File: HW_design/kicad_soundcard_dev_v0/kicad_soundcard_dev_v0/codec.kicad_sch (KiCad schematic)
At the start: 54 parts, among them J8 PJ31060-I, J9 PJ31060-I, Q3 BSS138LT3G, Q4 BSS138LT3G, U6 ES8388

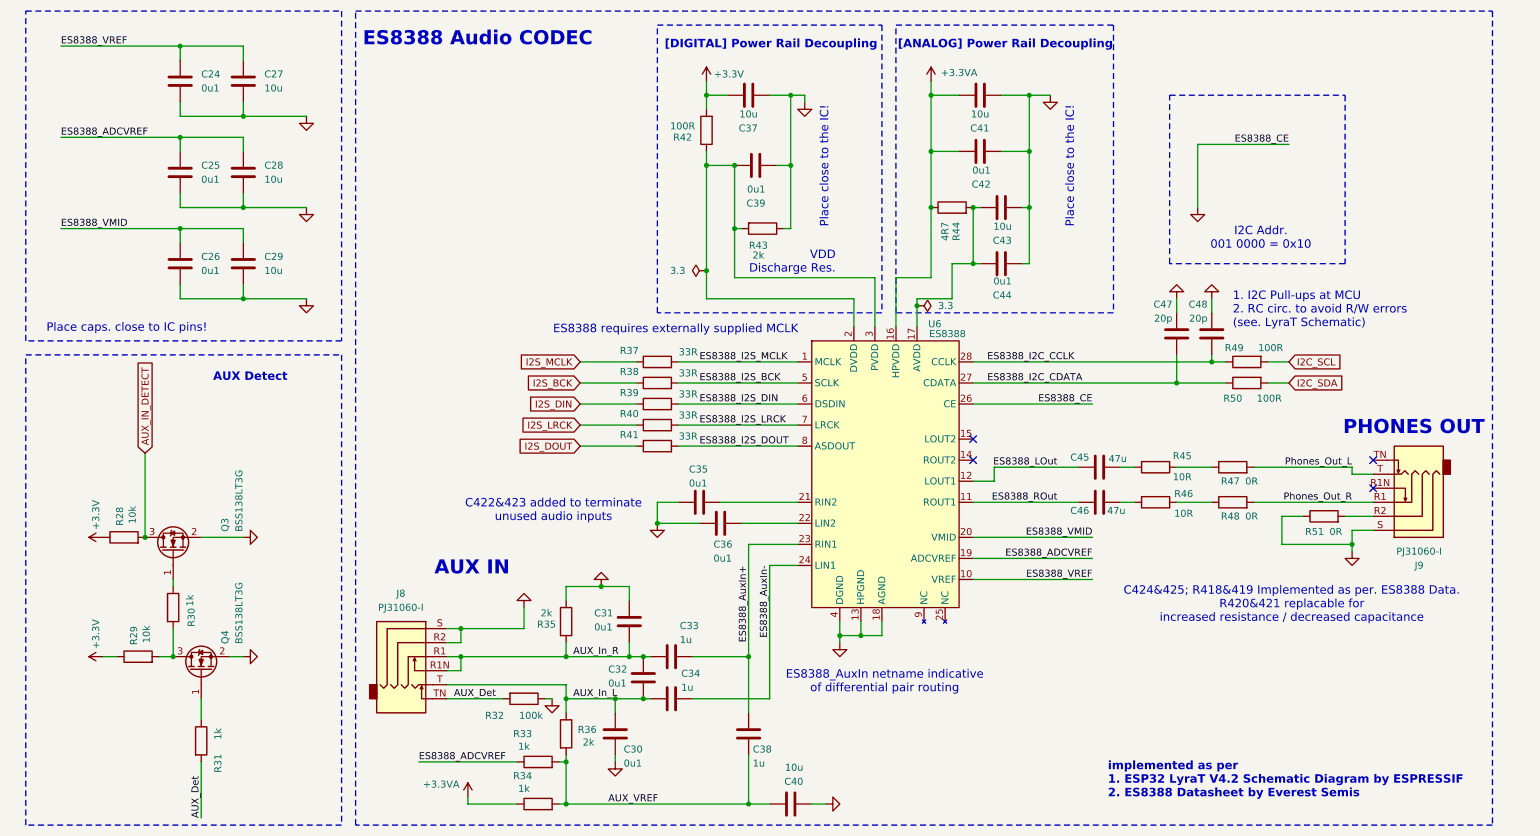
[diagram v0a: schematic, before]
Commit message: Schematic Rev2 + PCB Initial Release
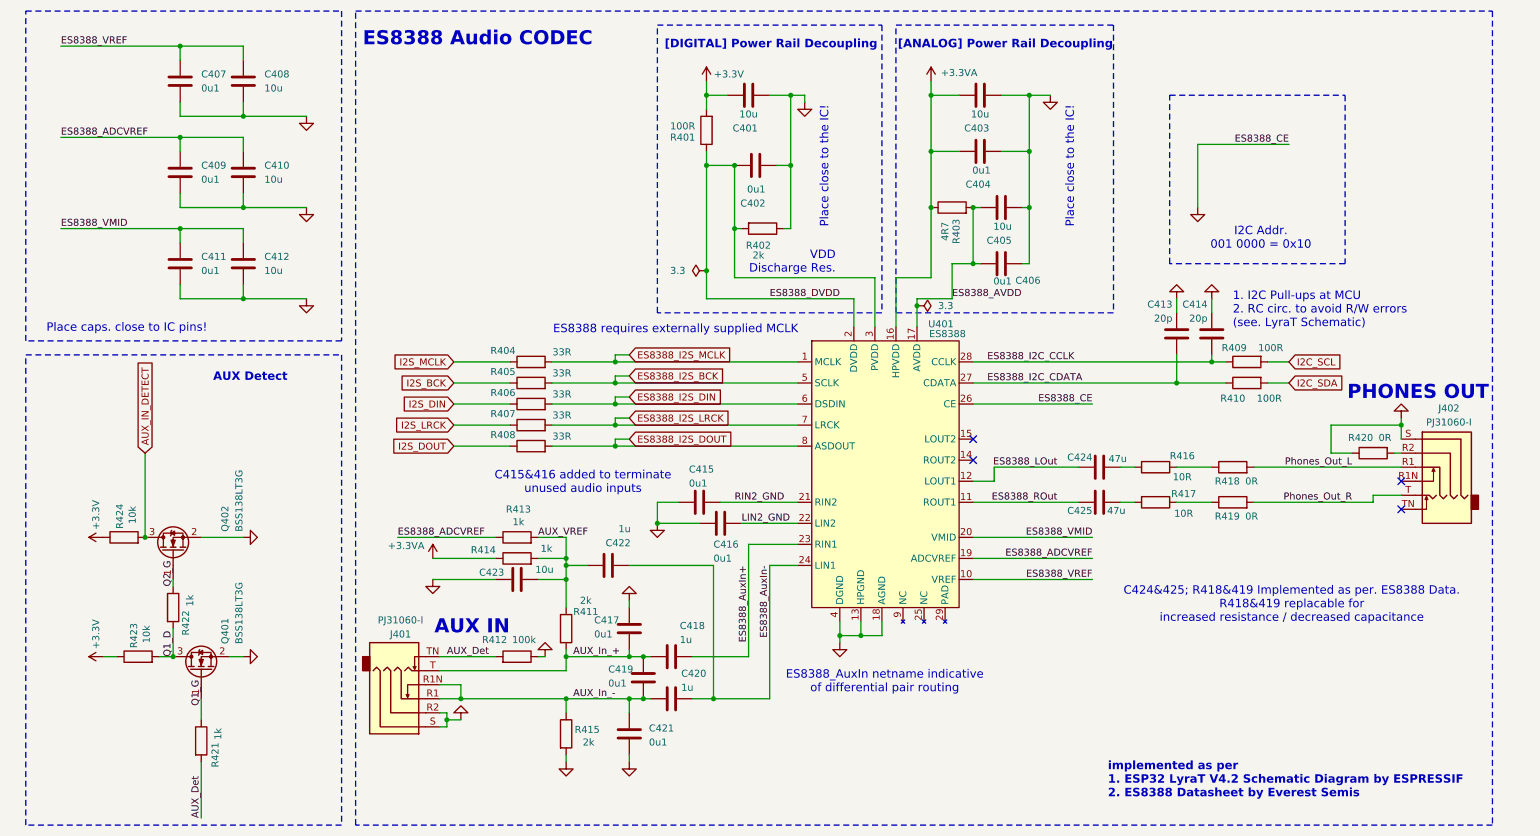
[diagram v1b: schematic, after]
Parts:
- removed R32: 100k, Resistor_SMD:R_0402_1005Metric, symbol Device:R
- added R412: 100k, Resistor_SMD:R_0402_1005Metric, symbol Device:R
- renumbered C37 to C401, C39 to C402, C41 to C403, C42 to C404, C43 to C405, C44 to C406, C24 to C407, C27 to C408, C25 to C409, C28 to C410, C26 to C411, C29 to C412, C47 to C413, C48 to C414, C35 to C415, C36 to C416, C31 to C417, C33 to C418, C32 to C419, C34 to C420, C30 to C421, C38 to C422, C40 to C423, C45 to C424, C46 to C425, J8 to J401, J9 to J402, Q4 to Q401, Q3 to Q402, R42 to R401, R43 to R402, R44 to R403, R37 to R404, R38 to R405, R39 to R406, R40 to R407, R41 to R408, R49 to R409, R50 to R410, R35 to R411, R33 to R413, R34 to R414, R36 to R415, R45 to R416, R46 to R417, R47 to R418, R48 to R419, R51 to R420, R31 to R421, R30 to R422, R29 to R423, R28 to R424, U6 to U401
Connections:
- net AUX_Det: now also R412.2
- net AUX_VREF: now also C422.1, R411.1; no longer C422.2, R415.2
- net ES8388_AuxIn+: no longer C422.1
- net ES8388_AuxIn-: now also C422.2
- net GND: now also R415.2, R412.1; no longer R411.1
- net Phones_Out_L: now also J402.R1; no longer J402.T
- net Phones_Out_R: now also J402.T; no longer J402.R1
- net ES8388_DVDD: now reaches C402.1, R401.1, R402.2, U401.2 (DVDD), U401.3 (PVDD)
- net Q1_G: now reaches Q401.1 (G), R421.1
- net ES8388_AVDD: now reaches C405.1, C406.1, R403.2, U401.17 (AVDD)
- net RIN2_GND: now reaches C415.1, U401.21 (RIN2)
- net LIN2_GND: now reaches C416.1, U401.22 (LIN2)
- net Q2_G: now reaches Q402.1 (G), R422.1
- net Q1_D: now reaches Q401.3 (D), R422.2, R423.2
- net AUX_In_L renamed AUX_In_-
- net AUX_In_-: now also J401.R1, J401.R1N; no longer J401.T
- net AUX_In_R renamed AUX_In_+
- net AUX_In_+: now also J401.T; no longer J401.R1, J401.R1N
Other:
- note added: "C415&416 added to terminate unused audio inputs"
- note added: "C424&425; R418&419 Implemented as per. ES8388 Data. R418&419 replacable for increased resistance / decreased capacitance"
- note removed: "C422&423 added to terminate unused audio inputs"
- note removed: "C424&425; R418&419 Implemented as per. ES8388 Data. R420&421 replacable for increased resistance / decreased capacitance"
- moved on the sheet: C417, C421, C422, C423, J401, J402, R404, R405, R406, R407, R408, R411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

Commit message: Production JLCPCB V0
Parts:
- C401, C403, C405, C408, C410, C412, C423: JLCPCB Link (none) -> https://jlcpcb.com/partdetail/2043-CL10A106MQ8NNNC/C1691; Manufacturer (none) -> Samsung Electro-Mechanics; Manufacturer P/N (none) -> CL10A106MQ8NNNC
- C402, C404, C406, C407, C409, C411, C415, C416, C417, C419, C421: JLCPCB Link (none) -> https://jlcpcb.com/partdetail/1877-CL05B104KO5NNNC/C1525; Manufacturer (none) -> Samsung Electro-Mechanics; Manufacturer P/N (none) -> CL05B104KO5NNNC
- C413, C414: JLCPCB Link (none) -> https://jlcpcb.com/partdetail/1906-0402CG200J500NT/C1554; Manufacturer (none) -> FH (Guangdong Fenghua Advanced Tech); Manufacturer P/N (none) -> 0402CG200J500NT
- C418, C420, C422: JLCPCB Link (none) -> https://jlcpcb.com/partdetail/15107-CL05A105KP5NNNC/C14445; Manufacturer (none) -> Samsung Electro-Mechanics; Manufacturer P/N (none) -> CL05A105KP5NNNC
- C424, C425: JLCPCB Link (none) -> https://jlcpcb.com/partdetail/152108-GRM188R60J476ME15D/C14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; Manufacturer (none) -> Murata Electronics; Manufacturer P/N (none) -> GRM188R60J476ME15D
- J401, J402: JLCPCB Link (none) -> https://jlcpcb.com/partdetail/Hooya-PJ31060/C2939583; Manufacturer (none) -> HOOYA; Manufacturer P/N (none) -> PJ-31060
- Q401, Q402: JLCPCB Link (none) -> https://jlcpcb.com/partdetail/Onsemi-BSS138LT3G/C83790; Manufacturer (none) -> onsemi; Manufacturer P/N (none) -> BSS138LT3G
- R401, R409, R410: JLCPCB Link (none) -> https://jlcpcb.com/partdetail/25881-0402WGJ0101TCE/C25138; Manufacturer (none) -> UNI-ROYAL(Uniroyal Elec); Manufacturer P/N (none) -> 0402WGJ0101TCE
- R402, R411, R415: JLCPCB Link (none) -> https://jlcpcb.com/partdetail/4516-0402WGF2001TCE/C4109; Manufacturer (none) -> UNI-ROYAL(Uniroyal Elec); Manufacturer P/N (none) -> 0402WGF2001TCE
- R403: JLCPCB Link (none) -> https://jlcpcb.com/partdetail/25864-0402WGF470KTCE/C25121; Manufacturer (none) -> UNI-ROYAL(Uniroyal Elec); Manufacturer P/N (none) -> 0402WGF470KTCE
- R404, R405, R406, R407, R408: JLCPCB Link (none) -> https://jlcpcb.com/partdetail/25848-0402WGF330JTCE/C25105; Manufacturer (none) -> UNI-ROYAL(Uniroyal Elec); Manufacturer P/N (none) -> 0402WGF330JTCE
- R412: JLCPCB Link (none) -> https://jlcpcb.com/partdetail/26484-0402WGF1003TCE/C25741; Manufacturer (none) -> UNI-ROYAL(Uniroyal Elec); Manufacturer P/N (none) -> 0402WGF1003TCE
- R413, R414, R421, R422: JLCPCB Link (none) -> https://jlcpcb.com/partdetail/12256-0402WGF1001TCE/C11702; Manufacturer (none) -> UNI-ROYAL(Uniroyal Elec); Manufacturer P/N (none) -> 0402WGF1001TCE
- R416, R417: JLCPCB Link (none) -> https://jlcpcb.com/partdetail/23586-0603WAF100JT5E/C22859; Manufacturer (none) -> UNI-ROYAL(Uniroyal Elec); Manufacturer P/N (none) -> 0603WAF100JT5E
- R418, R419, R420: JLCPCB Link (none) -> https://jlcpcb.com/partdetail/16080-0603WAJ0000T5E/C15402; Manufacturer (none) -> UNI-ROYAL(Uniroyal Elec); Manufacturer P/N (none) -> 0603WAJ0000T5E
- R423, R424: JLCPCB Link (none) -> https://jlcpcb.com/partdetail/26487-0402WGF1002TCE/C25744; Manufacturer (none) -> UNI-ROYAL(Uniroyal Elec); Manufacturer P/N (none) -> 0402WGF1002TCE
- U401: footprint Package_DFN_QFN:QFN-28-1EP_4x4mm_P0.4mm_EP2.6x2.6mm -> Package_DFN_QFN:QFN-28-1EP_4x4mm_P0.45mm_EP2.6x2.6mm; JLCPCB Link (none) -> https://jlcpcb.com/partdetail/339918-ES8388/C365736; Manufacturer (none) -> Everest-semi(Everest Semiconductor); Manufacturer P/N (none) -> ES8388
